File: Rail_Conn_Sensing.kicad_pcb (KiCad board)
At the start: 2 copper layers, 96.5 x 40.6 mm, 27 parts, among them J1 Rail Sensing Inputs, J2 Vin & GND, J3 Outputs, U1 AMC1200, U2 AMC1200, U3 MCP6004, U4 74LS00, U5 74LS86, U6 L7805

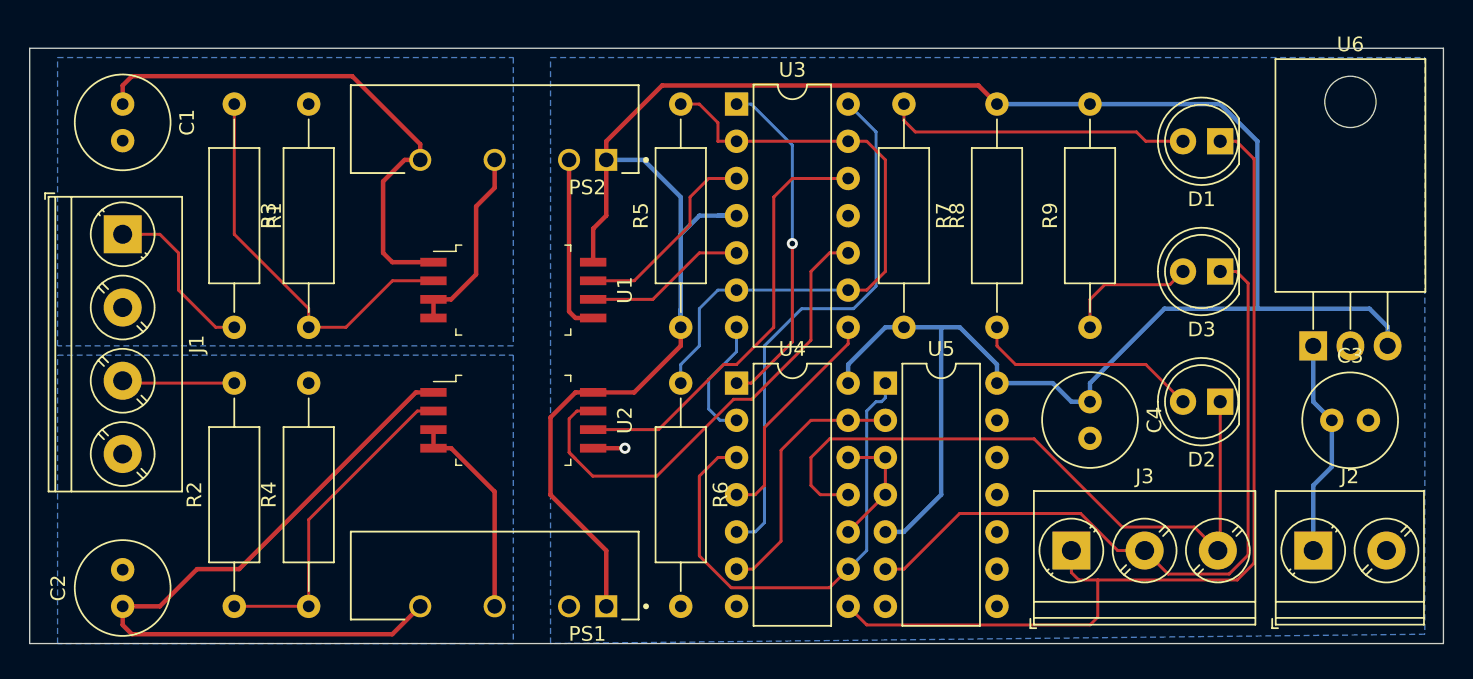
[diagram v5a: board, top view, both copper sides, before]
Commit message: Fix up wires and move silk screen labels
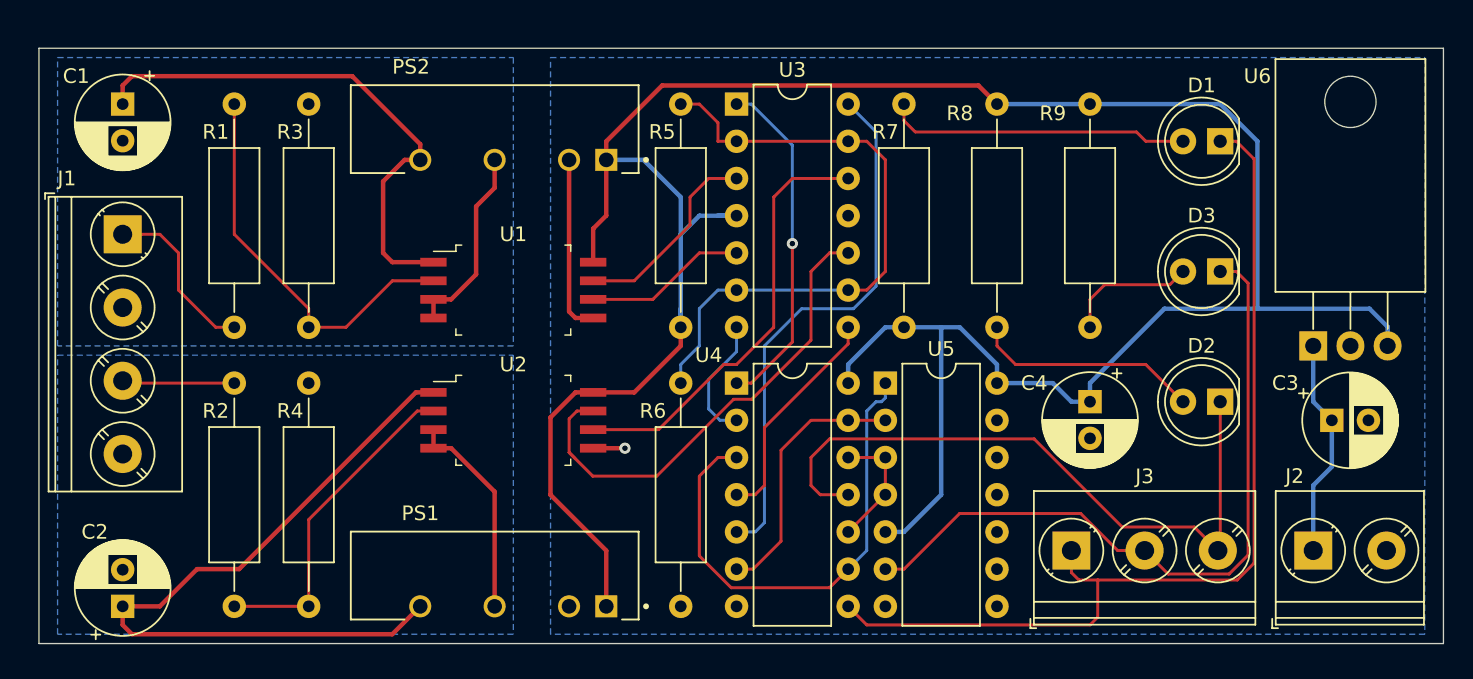
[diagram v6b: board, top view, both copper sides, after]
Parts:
- C1, C2, C3, C4: footprint Capacitor_THT:C_Radial_D6.3mm_H11.0mm_P2.50mm -> Capacitor_THT:CP_Radial_D6.3mm_P2.50mm
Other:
- board size 96.5 x 40.6 mm -> 95.9 x 40.6 mm

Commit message: Add connections to ground for floating unused input pins
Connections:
- U5 pad 10: (no net) -> GND
- U5 pad 11: (no net) -> Net-(U5-Pad11)
- U5 pad 12: (no net) -> GND
- U5 pad 13: (no net) -> GND
- U5 pad 8: (no net) -> Net-(U5-Pad8)
- U5 pad 9: (no net) -> GND
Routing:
- net Net-(R5-Pad2): track 43.3 -> 45.4 mm
- net Net-(U3-Pad14): track 36.8 -> 38.3 mm

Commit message: Add silkscreen for board name and input/output labels
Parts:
- moved J1 0.63 mm to (27.9, 50.2)
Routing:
- net Net-(R5-Pad2): track 45.4 -> 44.2 mm
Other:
- board text added: "+"
- board text added: "-"
- board text added: "1"
- board text added: "2"
- board text added: "3"
- board text added: "A"
- board text added: "B"
- board text added: "C"
- board text added: "D"
- board text added: "Inputs A & B"
- board text added: "Inputs C & D"
- board text added: "Ouputs"
- board text added: "Rail Conn Sensing v01 2020/07/10"
- board text added: "Vin"
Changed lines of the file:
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@@
   (general
     (thickness 1.6)
-    (drawings 4)
-    (tracks 250)
+    (drawings 18)
+    (tracks 249)
     (zones 0)
     (modules 27)
@@
   )
   (module TerminalBlock_Phoenix:TerminalBlock_Phoenix_PT-1,5-4-5.0-H_1x04_P5.00mm_Horizontal (layer F.Cu)
-    (at 27.94 49.53 270)
+    (at 27.94 50.165 270)
     (descr "Terminal Block Phoenix PT-1,5-4-5.0-H, 4 pins, pitch 5mm, size 20x9mm^2, drill diamater 1.3mm, pad diameter 2.6mm, see http://www.mouser.com/ds/2/324/ItemDetail_1935161-922578.pdf, script-generated using https://github.com/pointhi/kicad-footprint-generator/scripts/TerminalBlock_Phoenix")
     (tags "THT Terminal Block Phoenix PT-1,5-4-5.0-H pitch 5mm size 20x9mm^2 drill 1.3mm pad 2.6mm")
@@
     (descr "Terminal Block Phoenix PT-1,5-2-5.0-H, 2 pins, pitch 5mm, size 10x9mm^2, drill diamater 1.3mm, pad diameter 2.6mm, see http://www.mouser.com/ds/2/324/ItemDetail_1935161-922578.pdf, script-generated using https://github.com/pointhi/kicad-footprint-generator/scripts/TerminalBlock_Phoenix")
     (tags "THT Terminal Block Phoenix PT-1,5-2-5.0-H pitch 5mm size 10x9mm^2 drill 1.3mm pad 2.6mm")
-    (fp_text reference J2 (at -1.27 -5.08) (layer F.SilkS)
+    (fp_text reference J2 (at -2.286 -5.08) (layer F.SilkS)
       (effects (font (size 1 1) (thickness 0.15)))
     )
@@
     (descr "Terminal Block Phoenix PT-1,5-3-5.0-H, 3 pins, pitch 5mm, size 15x9mm^2, drill diamater 1.3mm, pad diameter 2.6mm, see http://www.mouser.com/ds/2/324/ItemDetail_1935161-922578.pdf, script-generated using https://github.com/pointhi/kicad-footprint-generator/scripts/TerminalBlock_Phoenix")
     (tags "THT Terminal Block Phoenix PT-1,5-3-5.0-H pitch 5mm size 15x9mm^2 drill 1.3mm pad 2.6mm")
-    (fp_text reference J3 (at 5 -5.06) (layer F.SilkS)
+    (fp_text reference J3 (at -3.048 -5.334) (layer F.SilkS)
       (effects (font (size 1 1) (thickness 0.15)))
     )
@@
       (rotate (xyz 0 0 0))
     )
+  )
+  (gr_text D (at 33.02 65.024) (layer F.SilkS)
+    (effects (font (size 1 1) (thickness 0.15)))
+  )
+  (gr_text C (at 33.02 60.96) (layer F.SilkS)
+    (effects (font (size 1 1) (thickness 0.15)))
+  )
+  (gr_text B (at 33.02 56.134) (layer F.SilkS)
+    (effects (font (size 1 1) (thickness 0.15)))
+  )
+  (gr_text A (at 33.02 50.038) (layer F.SilkS)
+    (effects (font (size 1 1) (thickness 0.15)))
+  )
+  (gr_text 3 (at 101.854 66.294) (layer F.SilkS)
+    (effects (font (size 1 1) (thickness 0.15)))
+  )
+  (gr_text 2 (at 97.536 66.294) (layer F.SilkS)
+    (effects (font (size 1 1) (thickness 0.15)))
+  )
+  (gr_text 1 (at 91.694 66.294) (layer F.SilkS)
+    (effects (font (size 1 1) (thickness 0.15)))
+  )
+  (gr_text Ouputs (at 97.536 74.93) (layer B.SilkS)
+    (effects (font (size 1 1) (thickness 0.15)) (justify mirror))
+  )
+  (gr_text + (at 108.458 65.278) (layer F.SilkS)
+    (effects (font (size 1 1) (thickness 0.15)))
+  )
+  (gr_text - (at 115.062 66.04) (layer F.SilkS)
+    (effects (font (size 1 1) (thickness 0.15)))
+  )
+  (gr_text Vin (at 112.014 74.676) (layer B.SilkS)
+    (effects (font (size 1 1) (thickness 0.15)) (justify mirror))
+  )
+  (gr_text "Inputs C & D" (at 24.638 64.008 90) (layer B.SilkS)
+    (effects (font (size 1 1) (thickness 0.15)) (justify mirror))
+  )
+  (gr_text "Inputs A & B" (at 24.638 51.816 90) (layer B.SilkS)
+    (effects (font (size 1 1) (thickness 0.15)) (justify mirror))
+  )
+  (gr_text "Rail Conn Sensing v01 \n2020/07/10" (at 39.878 69.596) (layer B.SilkS)
+    (effects (font (size 1 1) (thickness 0.15)) (justify mirror))
   )
   (gr_line (start 118.11 36.83) (end 22.225 36.83) (layer Edge.Cuts) (width 0.05))
@@
   (segment (start 80.01 52.07) (end 78.74 53.34) (width 0.2032) (layer F.Cu) (net 18))
   (segment (start 78.74 43.18) (end 80.01 44.45) (width 0.2032) (layer F.Cu) (net 18))
-  (segment (start 66.04 58.42) (end 66.04 59.69) (width 0.2032) (layer B.Cu) (net 18) (status 20))
   (segment (start 66.675 57.785) (end 66.04 58.42) (width 0.2032) (layer F.Cu) (net 18))
   (segment (start 69.85 53.34) (end 68.71863 53.34) (width 0.2032) (layer F.Cu) (net 18))
@@
     (polygon
       (pts
-        (xy 54.61 57.15) (xy 23.495 57.15) (xy 23.495 37.465) (xy 54.61 37.465)
+        (xy 54.61 57.404) (xy 22.86 57.404) (xy 22.86 37.465) (xy 54.61 37.465)
       )
     )
@@
     (polygon
       (pts
-        (xy 54.61 76.835) (xy 23.495 76.835) (xy 23.495 57.785) (xy 54.61 57.785)
+        (xy 54.61 76.835) (xy 22.86 76.835) (xy 22.86 58.166) (xy 54.4195 58.166)
       )
     )
@@
       )
     )
-  )
-  (zone (net 4) (net_name "Net-(C2-Pad2)") (layer B.Cu) (hatch edge 0.508)
-    (connect_pads (clearance 0.508))
-    (min_thickness 0.254)
-    (fill yes (arc_segments 32) (thermal_gap 0.508) (thermal_bridge_width 0.508))
-    (polygon
-      (pts
-        (xy 24.13 76.835) (xy 22.86 76.835) (xy 22.86 57.785) (xy 24.13 57.785)
-      )
-    )
-  )
-  (zone (net 2) (net_name "Net-(C1-Pad2)") (layer B.Cu) (hatch edge 0.508)
-    (connect_pads (clearance 0.508))
-    (min_thickness 0.254)
-    (fill yes (arc_segments 32) (thermal_gap 0.508) (thermal_bridge_width 0.508))
-    (polygon
-      (pts
-        (xy 24.13 57.15) (xy 22.86 57.15) (xy 22.86 37.465) (xy 24.13 37.465)
-      )
-    )
